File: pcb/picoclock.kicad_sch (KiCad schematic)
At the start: 70 parts, among them J1 UART, J10 USB, J11 Alt Power, J12 PWM, J13 AUDIO, J2 AUDIO, J3 xx, J4 xx, J5 Micro_SD_Card_Det1, J6 USB_C_Receptacle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

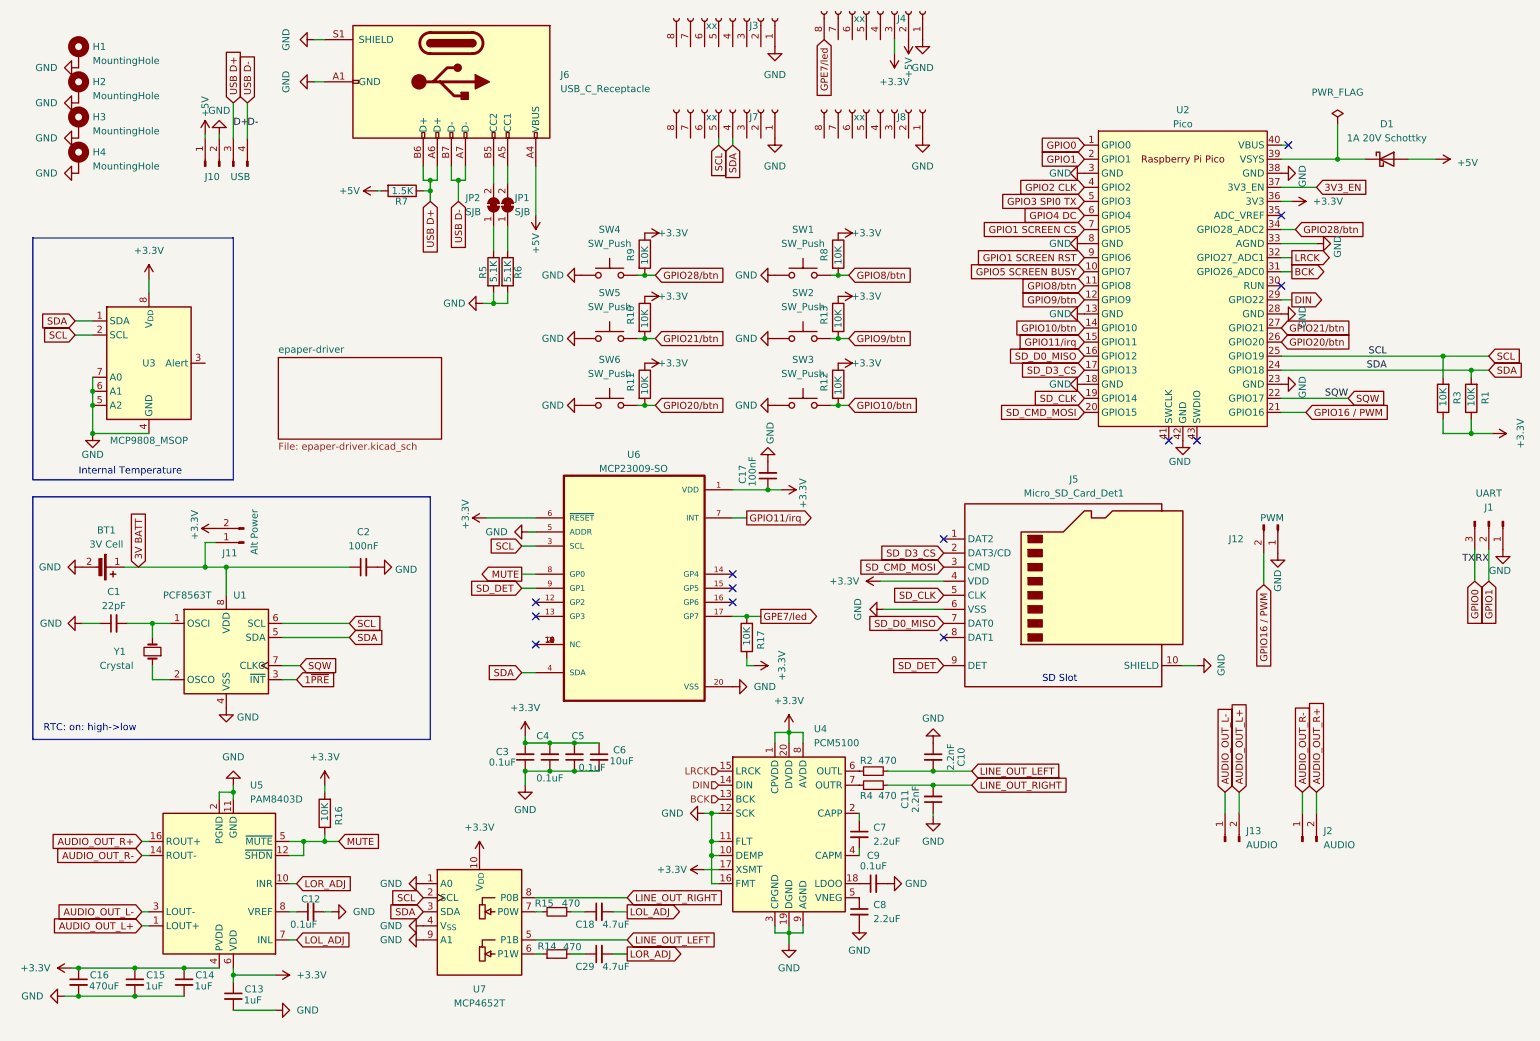
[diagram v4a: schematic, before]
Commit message: [pcb] move battery holder, other small tweaks
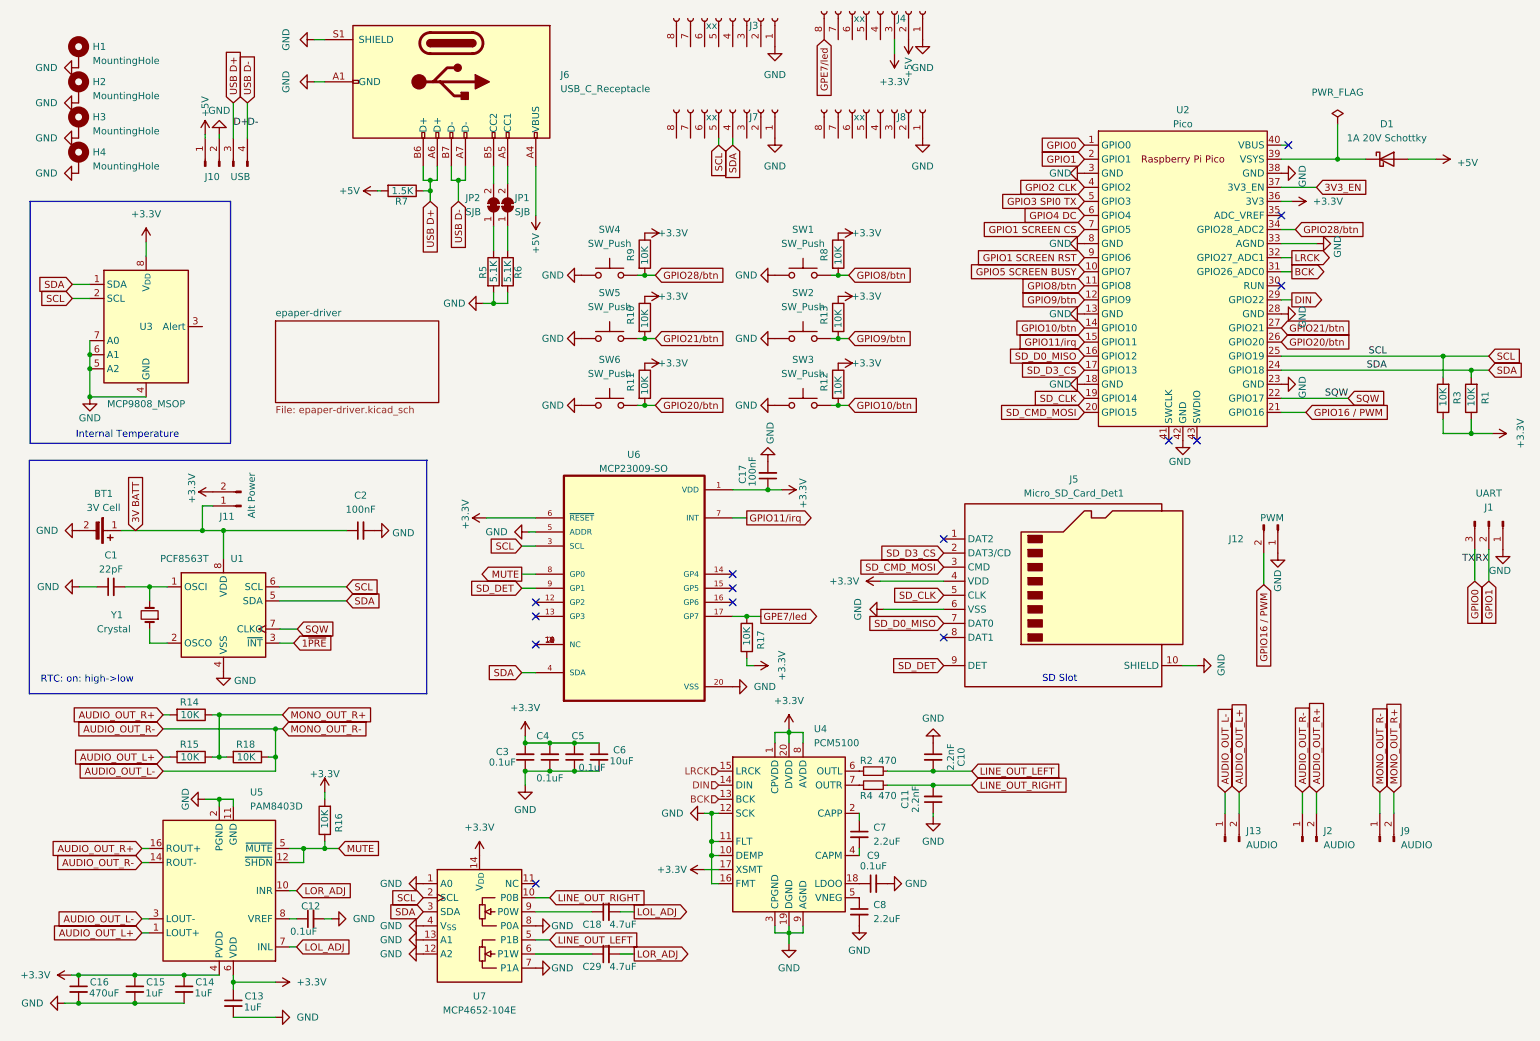
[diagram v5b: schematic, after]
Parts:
- removed R14, R15: 470, Resistor_SMD:R_0603_1608Metric, symbol Device:R_Small
- added J9: AUDIO, Connector_PinHeader_2.54mm:PinHeader_1x02_P2.54mm_Vertical, symbol Connector:Conn_01x02_Pin
- added R14, R15, R18: 10K, Resistor_SMD:R_0603_1608Metric, symbol Device:R
- U7: value MCP4652T -> MCP4652-104E; footprint Package_SO:MSOP-10_3x3mm_P0.5mm -> Package_SO:TSSOP-14_4.4x5mm_P0.65mm; symbol MCP4652:MCP4652T -> MCP4652:MCP4651T
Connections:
- net AUDIO_OUT_R- is gone; now on net AUDIO_OUT_L-: J2.1 (Pin_1), U5.14 (ROUT-)
- net +3.3V: now also U7.14 (V_{DD}); no longer U7.10 (V_{DD})
- net AUDIO_OUT_L+: now also R15.2
- net AUDIO_OUT_L-: now also J9.1 (Pin_1), R18.1
- net AUDIO_OUT_R+: now also R14.2
- net GND: now also U7.12 (A2), U7.13 (A1), U7.7 (P1A), U7.8 (P0A); no longer U7.9 (A1)
- net LINE_OUT_RIGHT: now also U7.10 (P0B); no longer U7.8 (P0B)
- net at C18.1: now also U7.9 (P0W)
- net at U7.6 (P1W): now also C29.1
- new net MONO_OUT_R+: J9.2 (Pin_2), R14.1, R15.1, R18.2
- no-connect marks 13 -> 14
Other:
- moved on the sheet: BT1, C1, C12, C13, C14, C15, C16, C18, C2, C29, J11, R16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

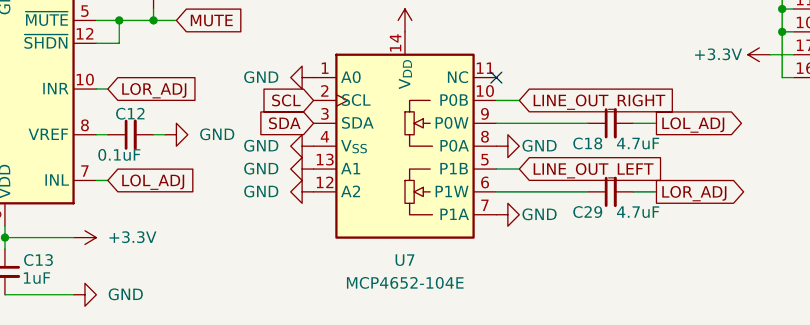
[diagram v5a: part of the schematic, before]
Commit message: [fw] big update: config support, split code
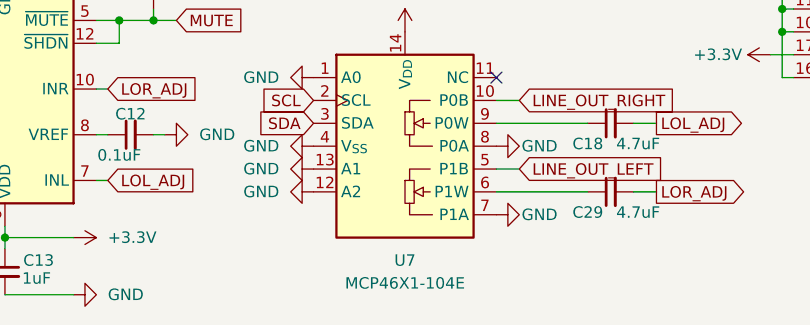
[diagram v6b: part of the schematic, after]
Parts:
- U7: value MCP4652-104E -> MCP46X1-104E
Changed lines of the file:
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@@
 	(label "SQW"
 		(at 252.095 83.82 180)
-		(fields_autoplaced yes)
 		(effects
 			(font
@@
 	(label "D-"
 		(at 53.34 34.925 0)
-		(fields_autoplaced yes)
 		(effects
 			(font
@@
 	(label "D+"
 		(at 50.8 34.925 0)
-		(fields_autoplaced yes)
 		(effects
 			(font
@@
 	(label "RX"
 		(at 277.495 113.665 180)
-		(fields_autoplaced yes)
 		(effects
 			(font
@@
 	(label "SCL"
 		(at 259.08 76.2 180)
-		(fields_autoplaced yes)
 		(effects
 			(font
@@
 	(label "SDA"
 		(at 259.08 78.74 180)
-		(fields_autoplaced yes)
 		(effects
 			(font
@@
 	(label "TX"
 		(at 274.955 113.665 180)
-		(fields_autoplaced yes)
 		(effects
 			(font
@@
 		(shape input)
 		(at 138.43 151.13 180)
-		(fields_autoplaced yes)
 		(effects
 			(font
@@
 		(shape input)
 		(at 138.43 153.67 180)
-		(fields_autoplaced yes)
 		(effects
 			(font
@@
 		(shape input)
 		(at 138.43 156.21 180)
-		(fields_autoplaced yes)
 		(effects
 			(font
@@
 			)
 		)
-		(property "Value" "MCP4652-104E"
+		(property "Value" "MCP46X1-104E"
 			(at 95.25 194.31 0)
 			(effects

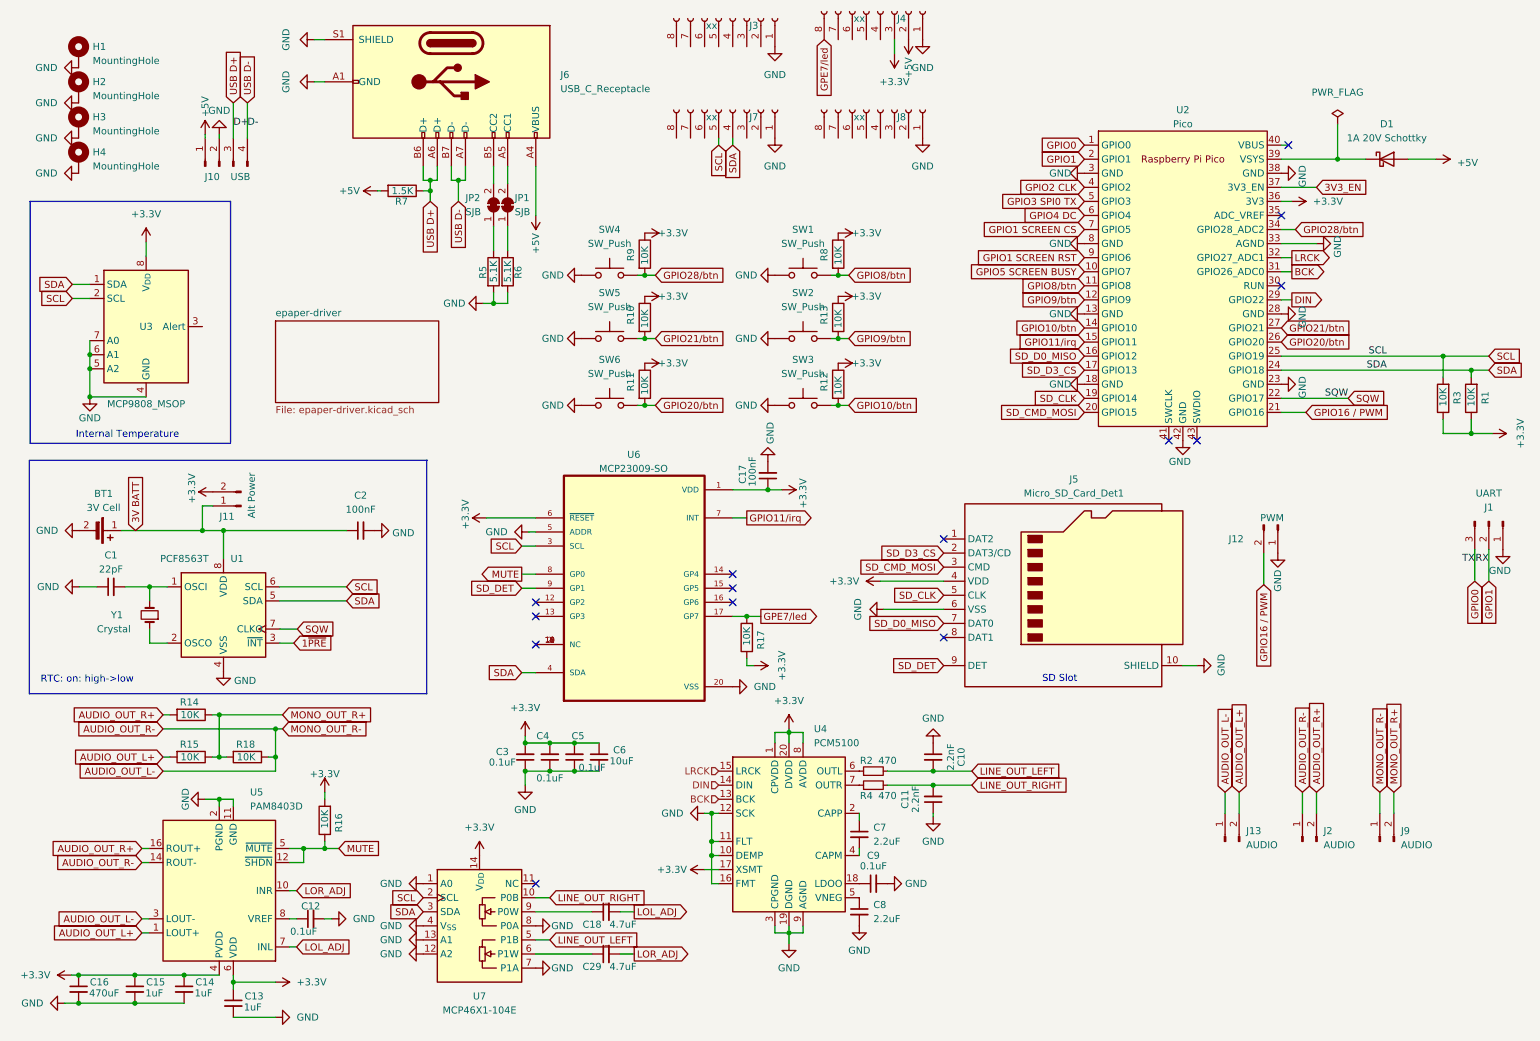
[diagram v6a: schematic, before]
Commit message: [pcb] mono audio, combined sdcard footprint
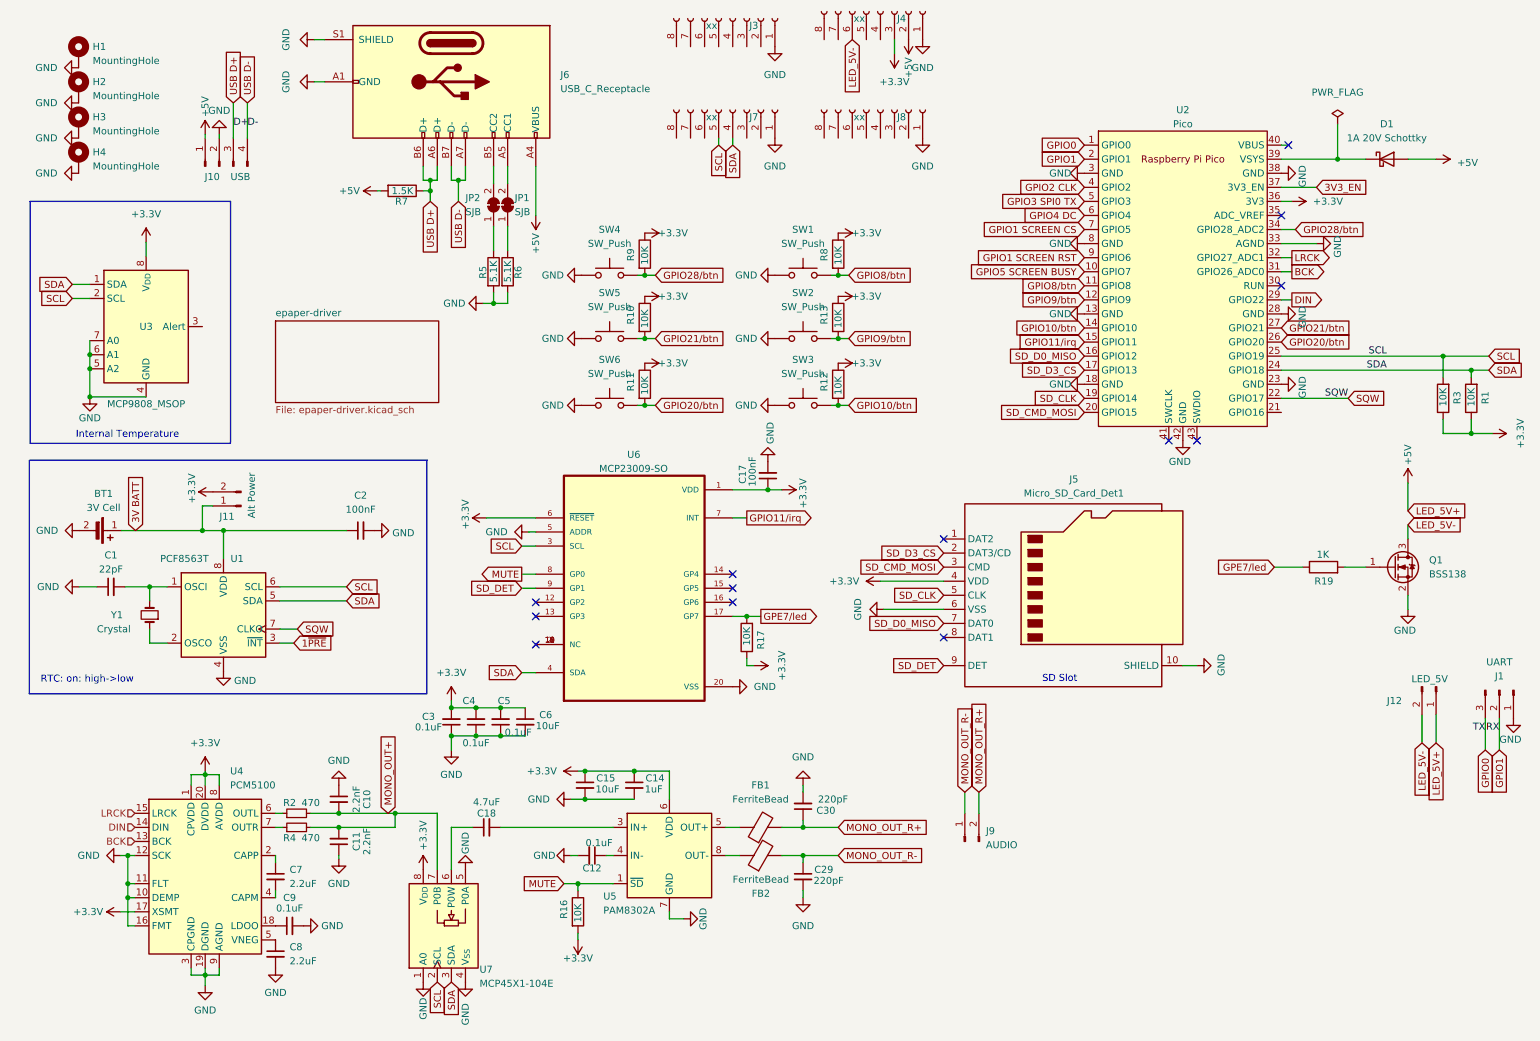
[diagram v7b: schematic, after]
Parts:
- removed C13: 1uF, Capacitor_SMD:C_0603_1608Metric, symbol Device:C_Small
- removed C16: 470uF, Capacitor_SMD:C_0603_1608Metric, symbol Device:C_Small
- removed J13, J2: AUDIO, Connector_PinHeader_2.54mm:PinHeader_1x02_P2.54mm_Vertical, symbol Connector:Conn_01x02_Pin
- removed R14, R15, R18: 10K, Resistor_SMD:R_0603_1608Metric, symbol Device:R
- added C30: 220pF, Capacitor_SMD:C_0603_1608Metric, symbol Device:C_Small
- added FB1, FB2: FerriteBead, Inductor_SMD:L_0603_1608Metric, symbol Device:FerriteBead
- added Q1: BSS138, Package_TO_SOT_SMD:SOT-23, symbol Transistor_FET:BSS138
- added R19: 1K, Resistor_SMD:R_0603_1608Metric, symbol Device:R
- C15: value 1uF -> 10uF
- C29: value 4.7uF -> 220pF
- C7: footprint Capacitor_SMD:C_0402_1005Metric -> Capacitor_SMD:C_0603_1608Metric
- H1, H2, H3, H4: footprint MountingHole:MountingHole_3mm_Pad -> MountingHole:MountingHole_3.2mm_M3_Pad
- J12: value PWM -> LED_5V
- J5: footprint Connector_Card:microSD_HC_Hirose_DM3AT-SF-PEJM5 -> clock:microSD_HC_Hirose_DM3AT-SF-PEJM5_combined_MSD-4-A
- SW1, SW2, SW3, SW4, SW5, SW6: footprint Button_Switch_SMD:SW_SPST_PTS645 -> clock:SW_SPST_TL3301TG
- U5: value PAM8403D -> PAM8302A; footprint Package_SO:SOP-16_3.9x9.9mm_P1.27mm -> Package_SO:SOP-8_3.76x4.96mm_P1.27mm; symbol Amplifier_Audio:PAM8403D -> Amplifier_Audio:PAM8302AAD
- U7: value MCP46X1-104E -> MCP45X1-104E; footprint Package_SO:TSSOP-14_4.4x5mm_P0.65mm -> Package_SO:MSOP-8_3x3mm_P0.65mm; symbol MCP4652:MCP4651T -> MCP4652:MCP4551T
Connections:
- net AUDIO_OUT_L+ is gone; now on net MUTE: U5.1 (~{SD})
- net +3.3V: now also U7.8 (V_{DD}); no longer U5.13 (PVDD), U5.4 (PVDD), U7.14 (V_{DD})
- net +5V: now also J12.1 (Pin_1)
- net GND: now also C29.2, U5.7 (GND), U7.5 (P0A), C30.2, Q1.2 (S); no longer J12.1 (Pin_1), U5.11 (GND), U5.15 (PGND), U5.2 (PGND), U7.12 (A2), U7.13 (A1), U7.7 (P1A), U7.8 (P0A)
- net GPE7/led: now also R19.1; no longer J4.8 (Pin_8)
- net MONO_OUT_R+: now also C30.1, FB1.2
- net MUTE: no longer U5.12 (~{SHDN}), U5.5 (~{MUTE})
- net at C18.1: now also U7.6 (P0W); no longer U7.9 (P0W)
- net MONO_OUT_R-: now reaches C29.1
- net MONO_OUT_R-: now also J9.1 (Pin_1), FB2.2; no longer U7.6 (P1W)
- net at C12.1: now also U5.4 (IN-); no longer U5.8 (VREF)
- net LED_5V-: now reaches J4.6 (Pin_6)
- net LED_5V-: now also J12.2 (Pin_2), Q1.3 (D)
- removed net AUDIO_OUT_L-: J9.1 (Pin_1), U5.14 (ROUT-), U5.3 (LOUT-)
- removed net AUDIO_OUT_R+: U5.16 (ROUT+)
- net GPIO16 / PWM: no longer names the net of U2.21 (GPIO16)
- net GPIO16 / PWM: no longer J12.2 (Pin_2)
- net LINE_OUT_LEFT renamed MONO_OUT+
- net MONO_OUT+: now also C11.2, R4.2, U7.7 (P0B); no longer U7.5 (P1B)
- removed net LINE_OUT_RIGHT: C11.2, R4.2, U7.10 (P0B)
- net LOL_ADJ: no longer names the net of C18.2
- net LOL_ADJ: now also U5.3 (IN+); no longer U5.7 (INL)
- removed net LOR_ADJ: C29.2, U5.10 (INR)
- new net: FB1.1, U5.5 (OUT+)
- new net: FB2.1, U5.8 (OUT-)
- new net: Q1.1 (G), R19.2
- no-connect marks 14 -> 13
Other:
- moved on the sheet: C10, C11, C12, C14, C15, C18, C3, C4, C5, C6, C7, C8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

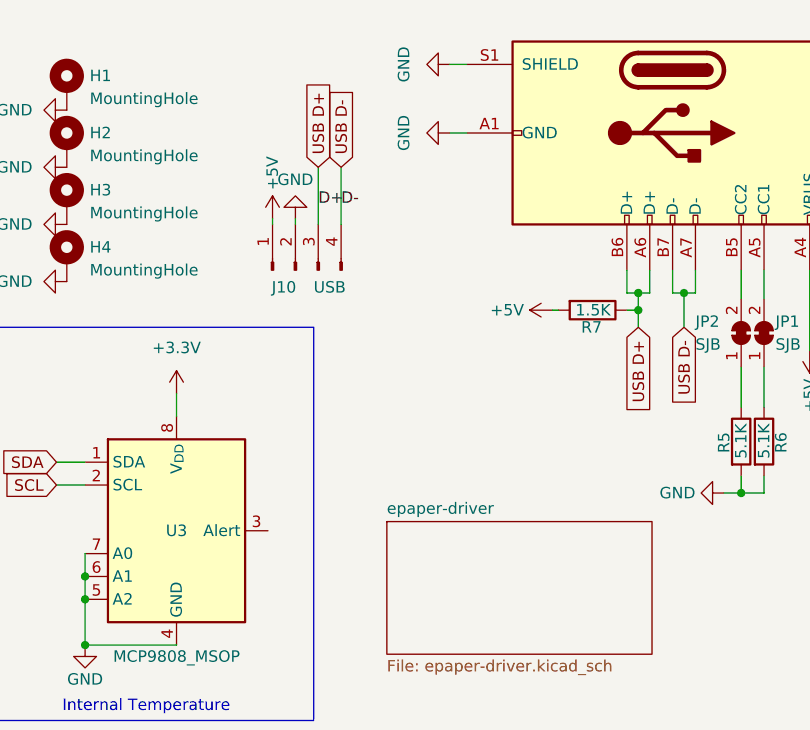
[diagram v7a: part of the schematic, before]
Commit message: [pcb] add USB-A
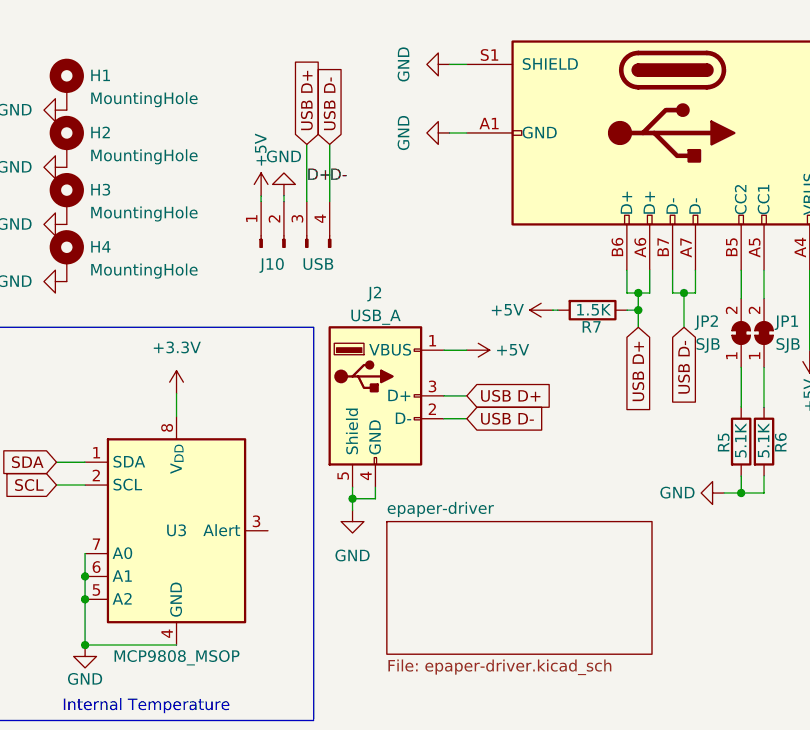
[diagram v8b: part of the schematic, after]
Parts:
- added J2: USB_A, Connector_USB:USB_A_Connfly_DS1095, symbol Connector:USB_A
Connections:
- net +5V: now also J2.1 (VBUS)
- net GND: now also J2.4 (GND), J2.5 (Shield)
- net USB D+: now also J2.3 (D+)
- net USB D-: now also J2.2 (D-)
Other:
- moved on the sheet: J10
